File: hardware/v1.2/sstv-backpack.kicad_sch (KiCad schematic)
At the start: 25 parts, among them J1 Conn_01x03_Pin, J2 Conn_01x02_Pin, J4 USB_C_Receptacle_USB2.0_14P, Q1 MMBT3904, SW1 SW_Push, SW2 SLW-1276864-4A-D, U1 ESP32-CAM, U2 FT231XS

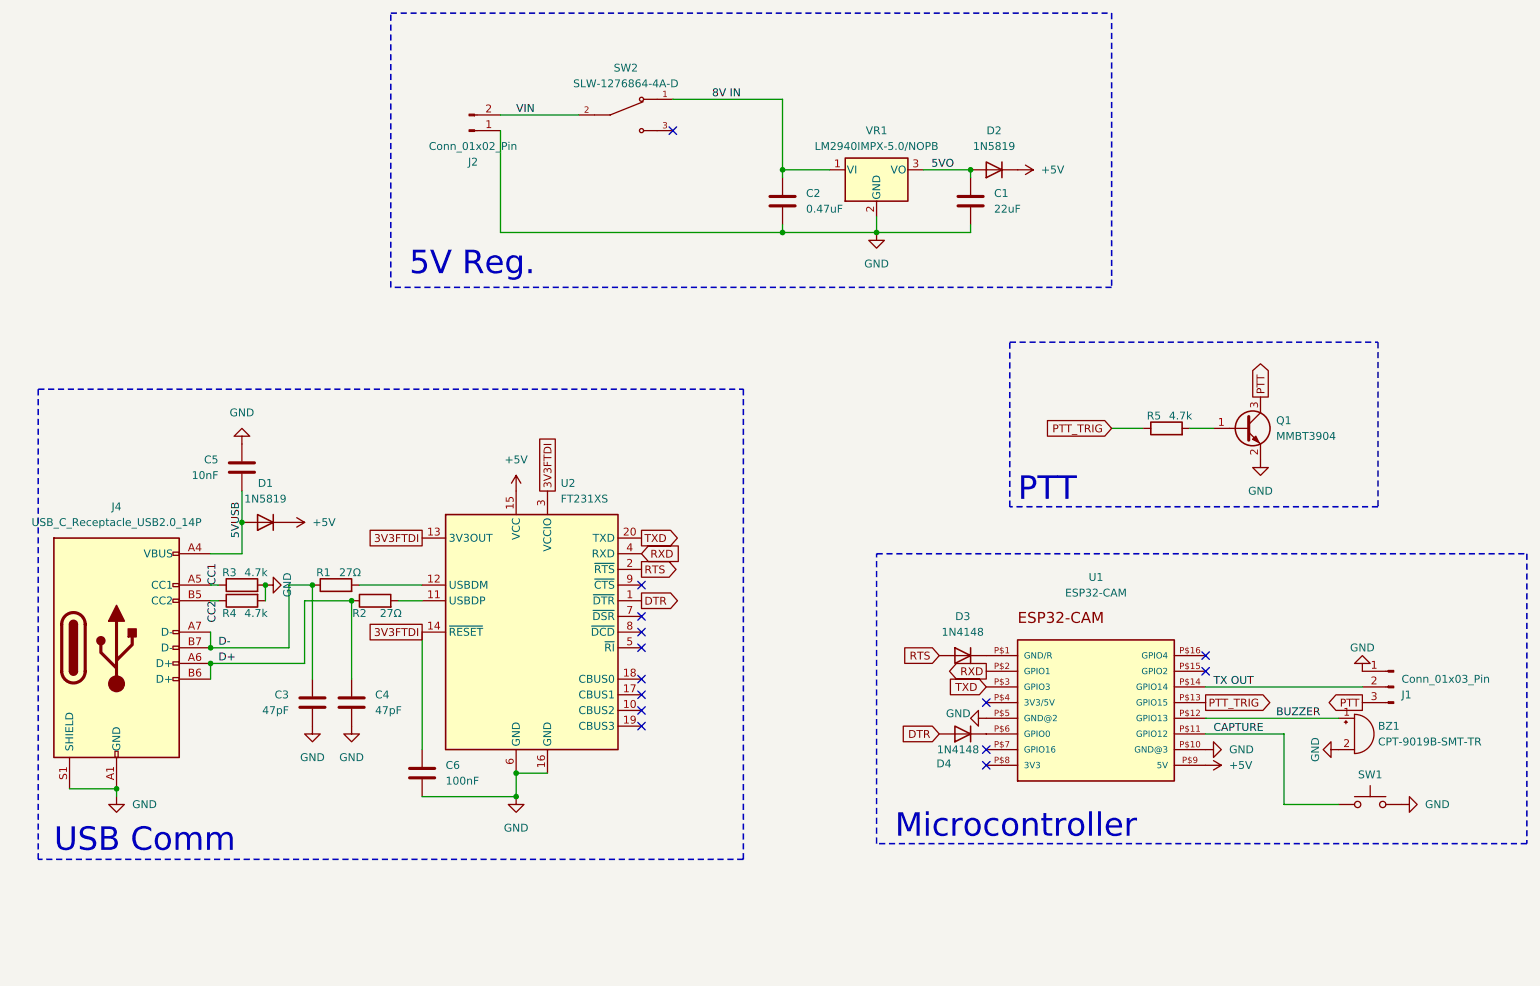
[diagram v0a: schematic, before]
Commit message: Update README and code for PTT
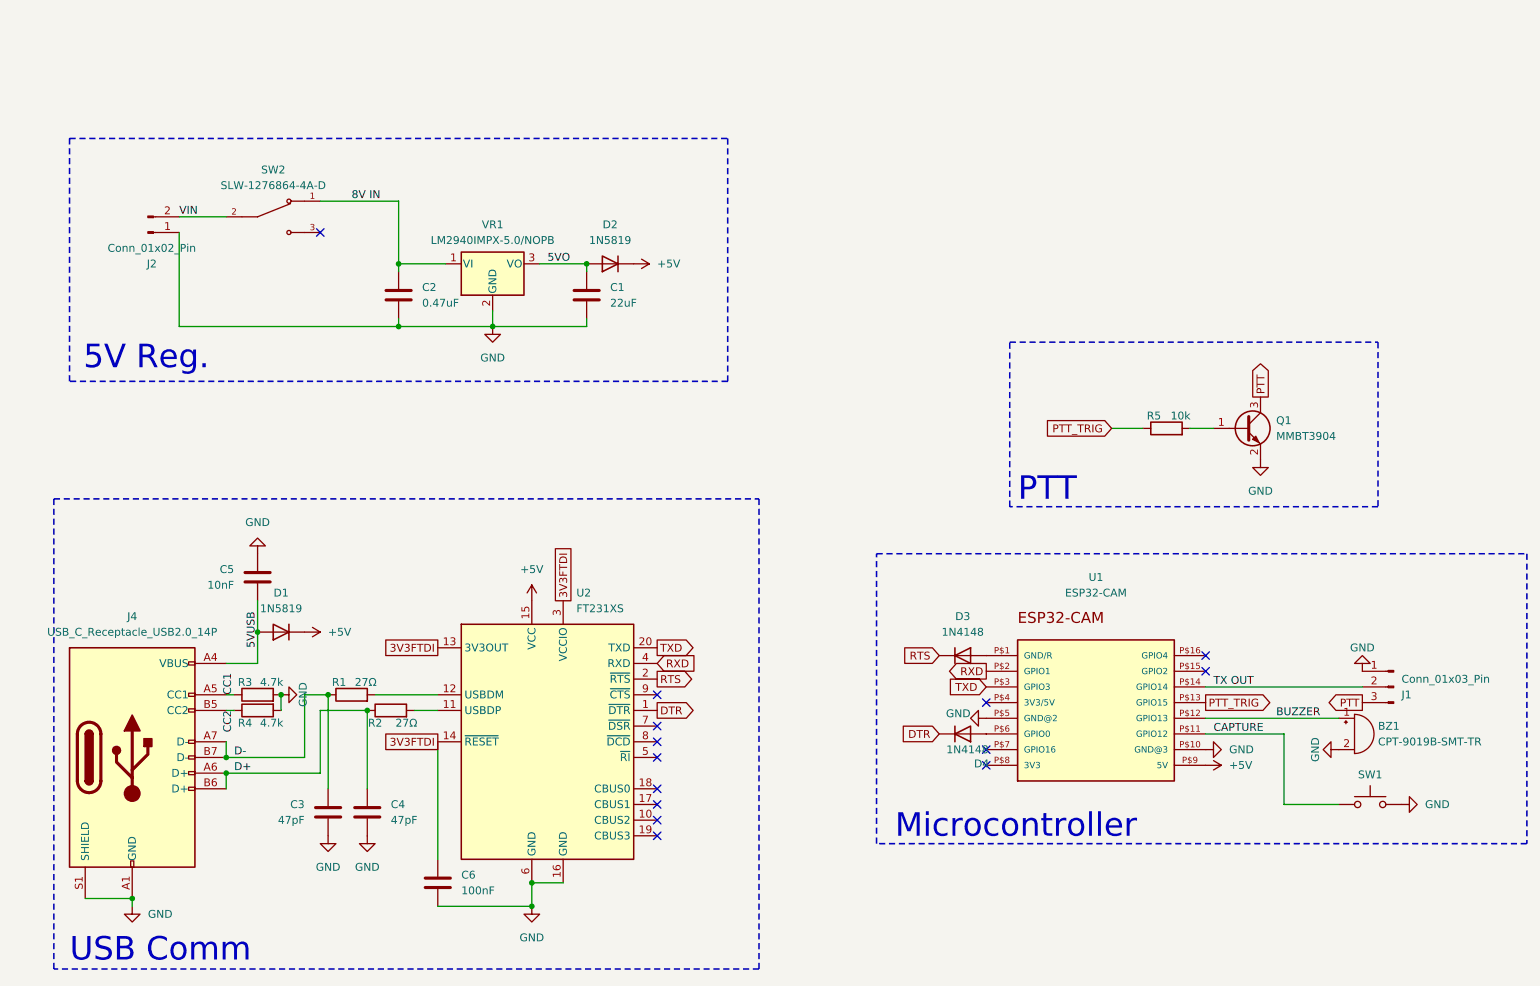
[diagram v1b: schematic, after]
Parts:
- R5: value 4.7k -> 10k
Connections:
- net DTR: now also D4.1 (K); no longer D4.2 (A)
- net RTS: now also D3.1 (K); no longer D3.2 (A)
- net at U1.P$1 (GND/R): now also D3.2 (A); no longer D3.1 (K)
- net at U1.P$6 (GPIO0): now also D4.2 (A); no longer D4.1 (K)
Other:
- moved on the sheet: C1, C2, C3, C4, C5, C6, D1, D2, D4, J2, J4, R1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
